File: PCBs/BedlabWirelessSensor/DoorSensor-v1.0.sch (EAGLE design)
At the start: 15 parts, among them U1 ATMEGA328P_PDIP

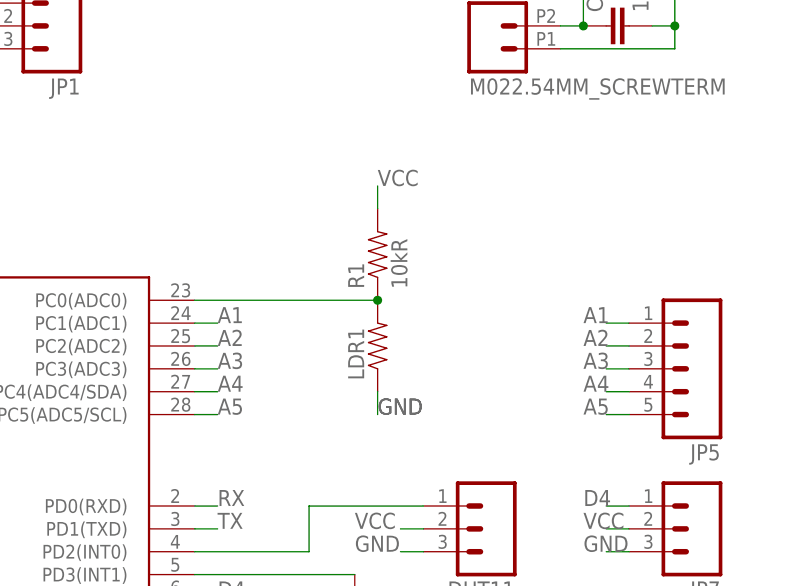
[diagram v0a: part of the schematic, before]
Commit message: Tiled PCB layout added for printing tomorrow. Additionally, changes made to arduino sketches to add funtionality for LDR, LED, Temp/humid sensor and switching the lights on/off from the gateway.
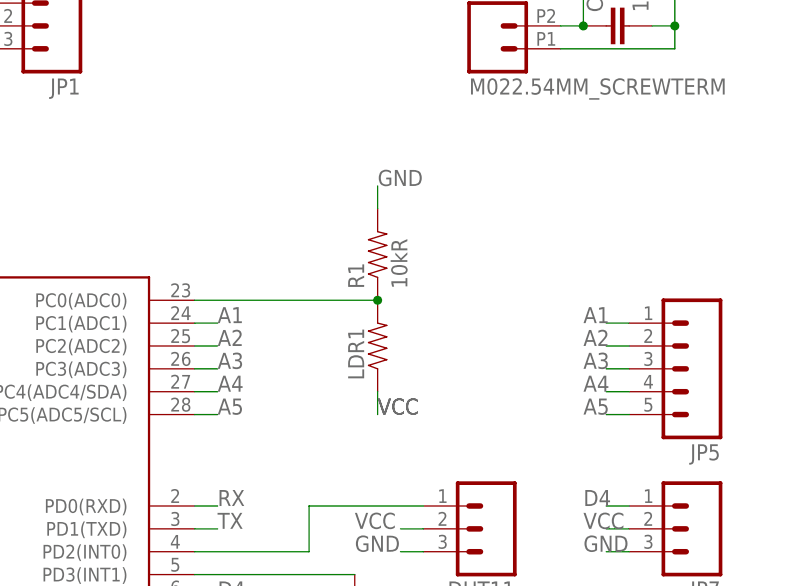
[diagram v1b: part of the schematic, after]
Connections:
- net GND: now also R1.2; no longer LDR1.1
- net VCC: now also LDR1.1; no longer R1.2
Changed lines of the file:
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@@
 <net name="VCC" class="0">
-<segment>
-<pinref part="R1" gate="G$1" pin="2"/>
-<wire x1="121.92" y1="83.82" x2="121.92" y2="86.36" width="0.1524" layer="91"/>
-<label x="121.92" y="86.36" size="1.778" layer="95"/>
-</segment>
 <segment>
 <pinref part="DHT11" gate="G$1" pin="2"/>
@@
 <label x="144.78" y="48.26" size="1.778" layer="95"/>
 </segment>
-</net>
-<net name="GND" class="0">
 <segment>
 <pinref part="LDR1" gate="G$1" pin="1"/>
@@
 <label x="121.92" y="60.96" size="1.778" layer="95"/>
 </segment>
+</net>
+<net name="GND" class="0">
 <segment>
 <pinref part="DHT11" gate="G$1" pin="3"/>
@@
 <label x="144.78" y="45.72" size="1.778" layer="95"/>
 </segment>
+<segment>
+<pinref part="R1" gate="G$1" pin="2"/>
+<wire x1="121.92" y1="83.82" x2="121.92" y2="86.36" width="0.1524" layer="91"/>
+<label x="121.92" y="86.36" size="1.778" layer="95"/>
+</segment>
 </net>
